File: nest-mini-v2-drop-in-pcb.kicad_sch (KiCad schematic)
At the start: 0 parts

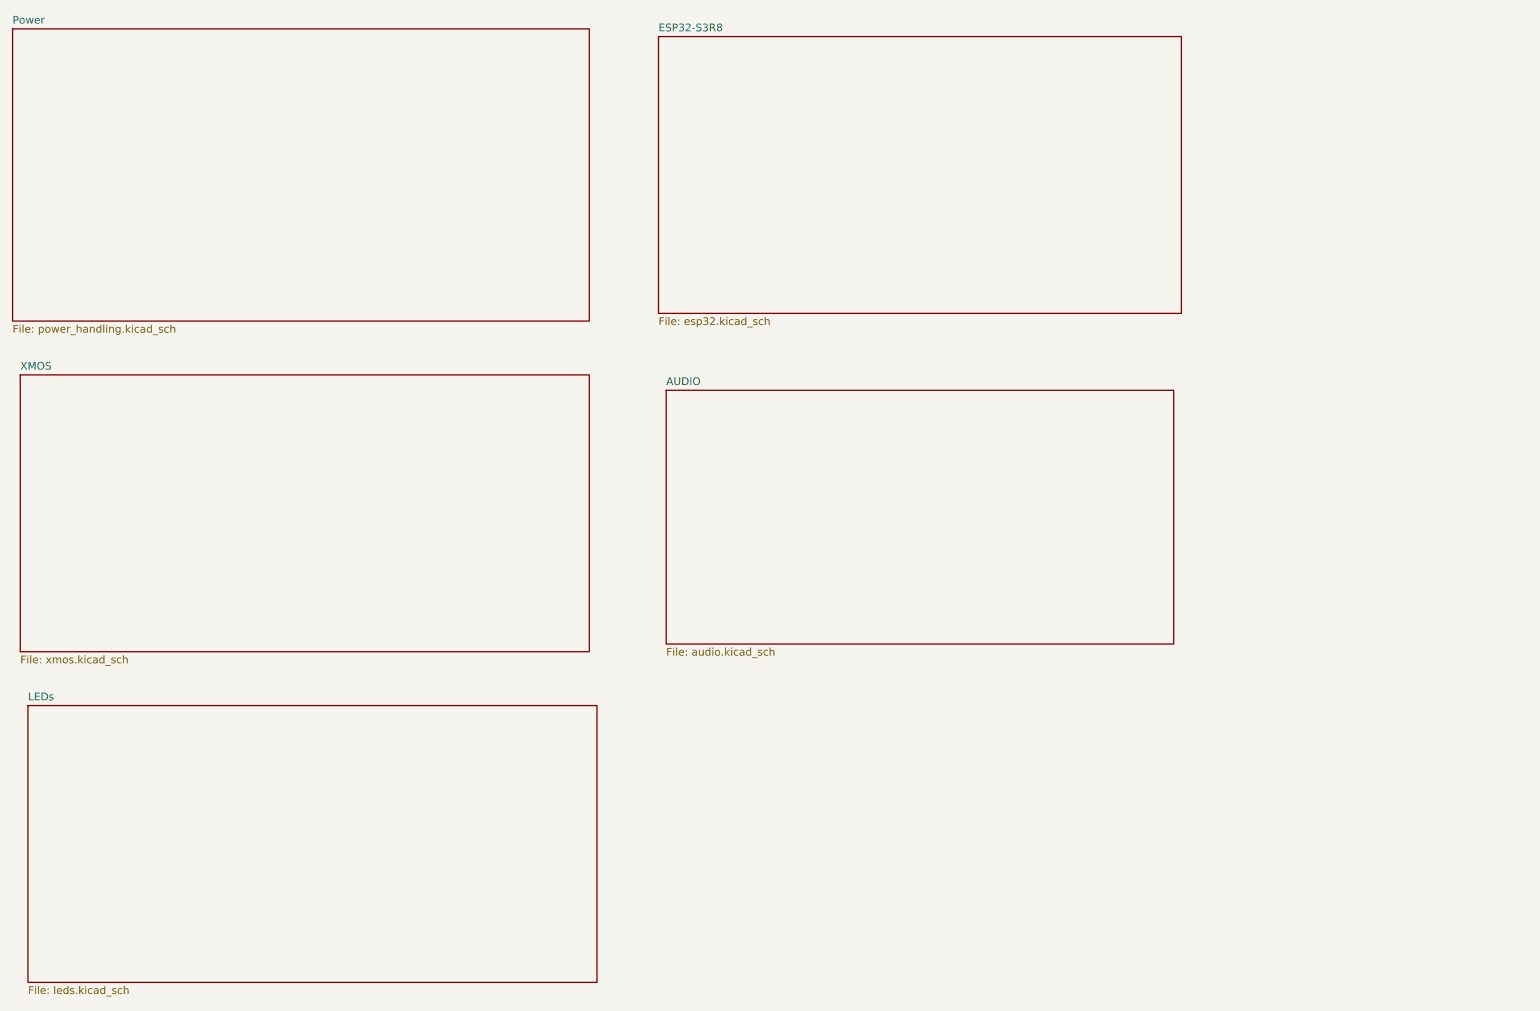
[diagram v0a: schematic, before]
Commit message: adding esp32c6 for OTBR
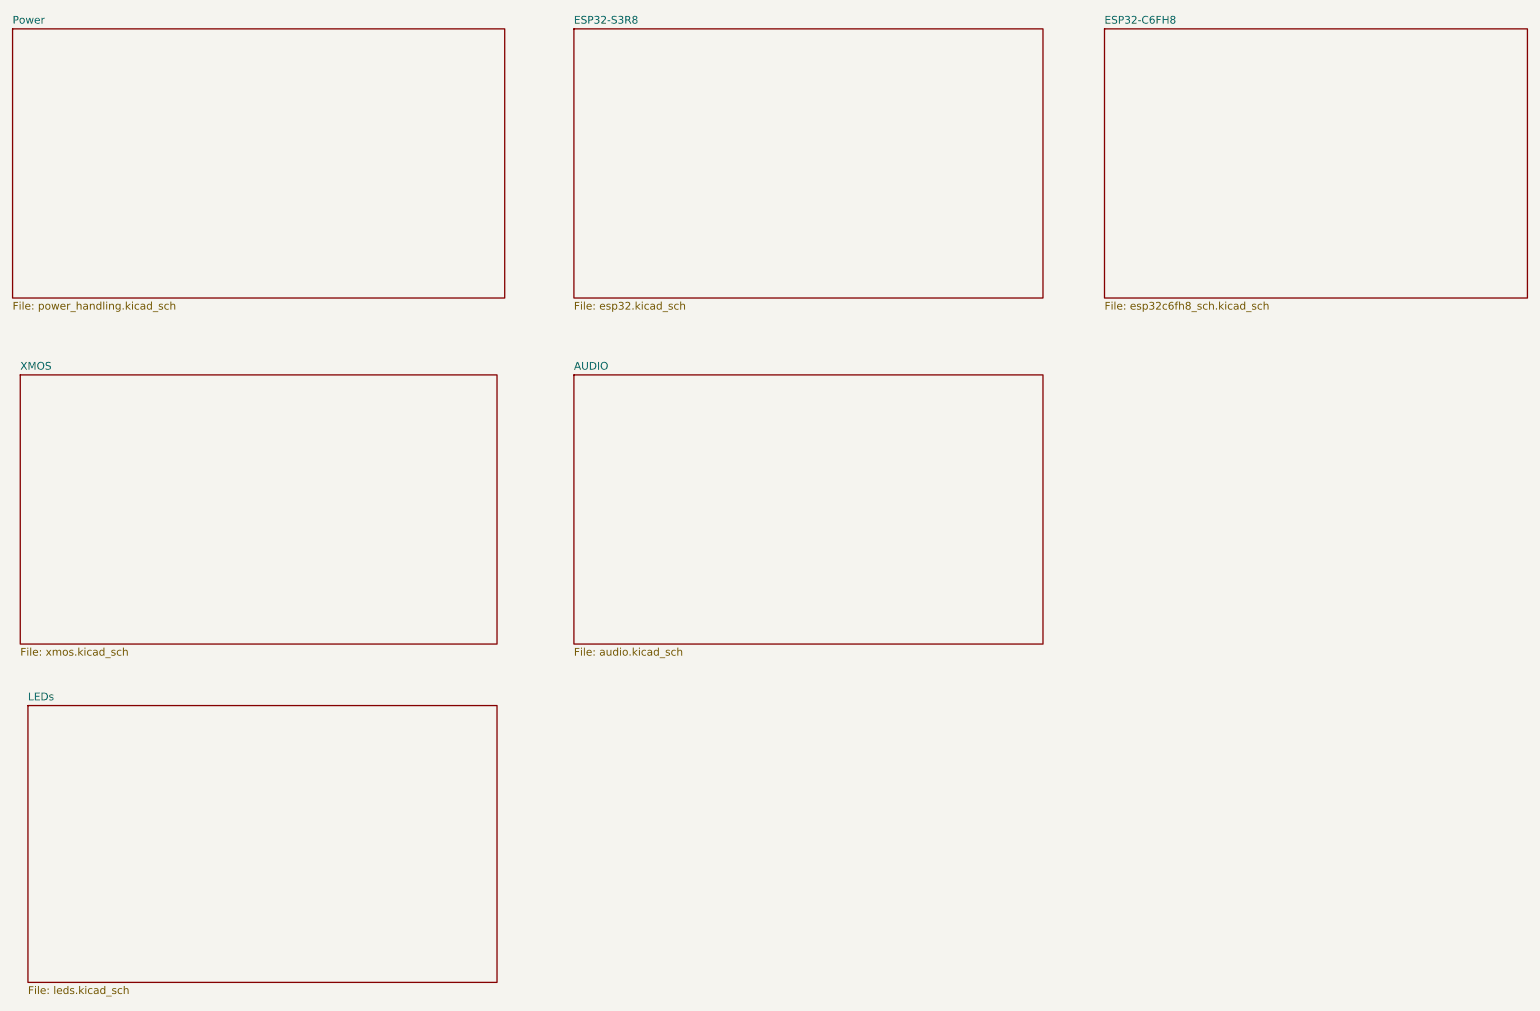
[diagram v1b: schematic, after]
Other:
- added sheet ESP32-C6FH8 (esp32c6fh8_sch.kicad_sch)
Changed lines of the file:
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@@
 	(sheet
 		(at 31.75 132.08)
-		(size 93.98 45.72)
+		(size 77.47 45.72)
 		(exclude_from_sim no)
 		(in_bom yes)
@@
 			(project "nest-mini-v2-drop-in-pcb"
 				(path "/204e071a-14ed-47a0-be54-332ac2b951cf"
-					(page "6")
+					(page "7")
 				)
 			)
@@
 	(sheet
 		(at 29.21 20.32)
-		(size 95.25 48.26)
+		(size 81.28 44.45)
 		(exclude_from_sim no)
 		(in_bom yes)
@@
 		)
 		(property "Sheetfile" "power_handling.kicad_sch"
-			(at 29.21 69.1646 0)
+			(at 29.21 65.3546 0)
 			(effects
 				(font
@@
 	)
 	(sheet
-		(at 137.16 80.01)
-		(size 83.82 41.91)
+		(at 121.92 77.47)
+		(size 77.47 44.45)
 		(exclude_from_sim no)
 		(in_bom yes)
@@
 		)
 		(property "Sheetname" "AUDIO"
-			(at 137.16 79.2984 0)
+			(at 121.92 76.7584 0)
 			(effects
 				(font
@@
 		)
 		(property "Sheetfile" "audio.kicad_sch"
-			(at 137.16 122.5046 0)
-			(effects
-				(font
-					(size 1.27 1.27)
-				)
-				(justify left top)
-			)
-		)
-		(instances
-			(project "nest-mini-v2-drop-in-pcb"
-				(path "/204e071a-14ed-47a0-be54-332ac2b951cf"
-					(page "5")
-				)
-			)
-		)
-	)
-	(sheet
-		(at 135.89 21.59)
-		(size 86.36 45.72)
+			(at 121.92 122.5046 0)
+			(effects
+				(font
+					(size 1.27 1.27)
+				)
+				(justify left top)
+			)
+		)
+		(instances
+			(project "nest-mini-v2-drop-in-pcb"
+				(path "/204e071a-14ed-47a0-be54-332ac2b951cf"
+					(page "6")
+				)
+			)
+		)
+	)
+	(sheet
+		(at 121.92 20.32)
+		(size 77.47 44.45)
 		(exclude_from_sim no)
 		(in_bom yes)
@@
 		)
 		(property "Sheetname" "ESP32-S3R8"
-			(at 135.89 20.8784 0)
+			(at 121.92 19.6084 0)
 			(effects
 				(font
@@
 		)
 		(property "Sheetfile" "esp32.kicad_sch"
-			(at 135.89 67.8946 0)
+			(at 121.92 65.3546 0)
 			(effects
 				(font
@@
 	)
 	(sheet
+		(at 209.55 20.32)
+		(size 69.85 44.45)
+		(exclude_from_sim no)
+		(in_bom yes)
+		(on_board yes)
+		(dnp no)
+		(fields_autoplaced yes)
+		(stroke
+			(width 0.1524)
+			(type solid)
+		)
+		(fill
+			(color 0 0 0 0.0000)
+		)
+		(property "Sheetname" "ESP32-C6FH8"
+			(at 209.55 19.6084 0)
+			(effects
+				(font
+					(size 1.27 1.27)
+				)
+				(justify left bottom)
+			)
+		)
+		(property "Sheetfile" "esp32c6fh8_sch.kicad_sch"
+			(at 209.55 65.3546 0)
+			(effects
+				(font
+					(size 1.27 1.27)
+				)
+				(justify left top)
+			)
+		)
+		(instances
+			(project "nest-mini-v2-drop-in-pcb"
+				(path "/204e071a-14ed-47a0-be54-332ac2b951cf"
+					(page "4")
+				)
+			)
+		)
+	)
+	(sheet
 		(at 30.48 77.47)
-		(size 93.98 45.72)
+		(size 78.74 44.45)
 		(exclude_from_sim no)
 		(in_bom yes)
@@
 		)
 		(property "Sheetfile" "xmos.kicad_sch"
-			(at 30.48 123.7746 0)
-			(effects
-				(font
-					(size 1.27 1.27)
-				)
-				(justify left top)
-			)
-		)
-		(instances
-			(project "nest-mini-v2-drop-in-pcb"
-				(path "/204e071a-14ed-47a0-be54-332ac2b951cf"
-					(page "4")
-				)
-			)
+			(at 30.48 122.5046 0)
+			(effects
+				(font
+					(size 1.27 1.27)
+				)
+				(justify left top)
+			)
+		)
+		(instances
+			(project "nest-mini-v2-drop-in-pcb"
+				(path "/204e071a-14ed-47a0-be54-332ac2b951cf"
+					(page "5")
+				)
+			)

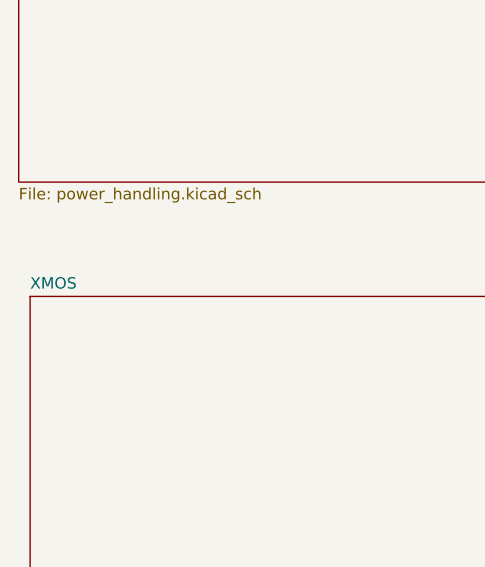
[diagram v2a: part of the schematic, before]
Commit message: Publish ESP32-P4 multi-sheet hardware redesign
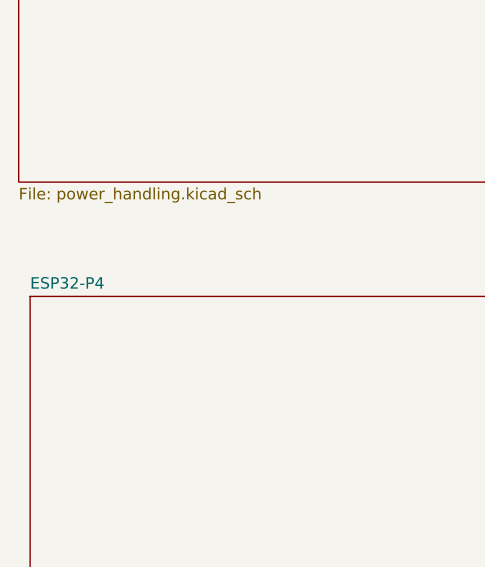
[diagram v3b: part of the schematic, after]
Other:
- sheet XMOS renamed ESP32-P4
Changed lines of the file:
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@@
 			(color 0 0 0 0)
 		)
-		(property "Sheetname" "XMOS"
+		(property "Sheetname" "ESP32-P4"
 			(at 30.48 76.7584 0)
 			(show_name no)
